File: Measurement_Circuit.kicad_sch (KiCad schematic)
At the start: 45 parts, among them IC1 ISO6721RBDR, J4 Screw_Terminal_01x03, J5 Screw_Terminal_01x03, J6 Screw_Terminal_01x02, U3 ADE7953xCP, U8 ISO1541, Y1 3.58 MHz

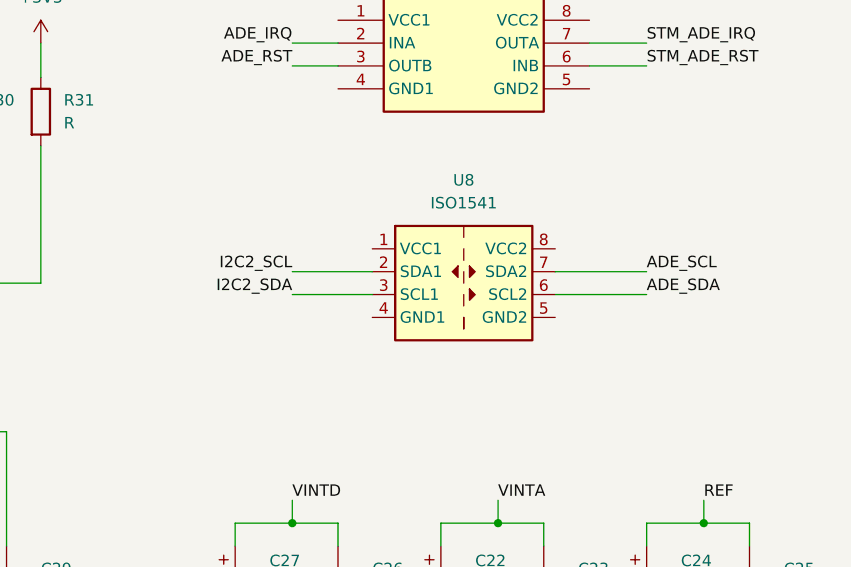
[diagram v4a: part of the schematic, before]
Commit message: I2C pullups
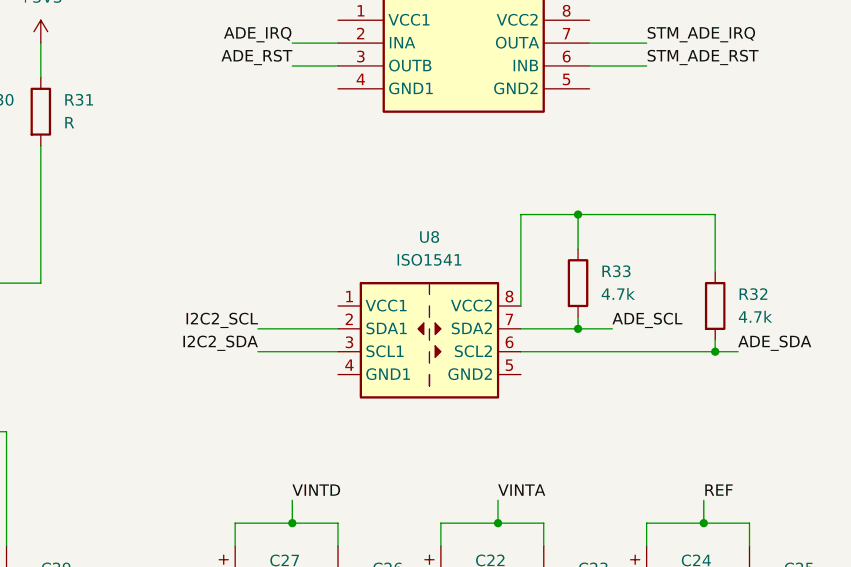
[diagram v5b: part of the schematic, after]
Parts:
- added R32, R33: 4.7k, symbol Device:R
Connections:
- net ADE_SCL: now also R33.2
- net ADE_SDA: now also R32.2
- net at U8.8 (VCC2): now also R32.1, R33.1
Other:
- moved on the sheet: U8
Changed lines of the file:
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@@
 (kicad_sch (version 20230121) (generator eeschema)
   (paper "A4")
+  (junction (at 236.22 64.77) (diameter 0) (color 0 0 0 0)
+  )
   (junction (at 158.75 99.06) (diameter 0) (color 0 0 0 0)
   )
@@
   (junction (at 63.5 55.88) (diameter 0) (color 0 0 0 0)
   )
+  (junction (at 251.46 80.01) (diameter 0) (color 0 0 0 0)
+  )
   (junction (at 78.74 44.45) (diameter 0) (color 0 0 0 0)
   )
@@
   )
   (junction (at 63.5 44.45) (diameter 0) (color 0 0 0 0)
+  )
+  (junction (at 236.22 77.47) (diameter 0) (color 0 0 0 0)
   )
   (junction (at 158.75 88.9) (diameter 0) (color 0 0 0 0)
@@
     (stroke (width 0) (type default))
   )
-  (wire (pts (xy 233.68 71.12) (xy 243.84 71.12))
+  (wire (pts (xy 229.87 77.47) (xy 236.22 77.47))
     (stroke (width 0) (type default))
   )
@@
     (stroke (width 0) (type default))
   )
+  (wire (pts (xy 251.46 80.01) (xy 254 80.01))
+    (stroke (width 0) (type default))
+  )
+  (wire (pts (xy 236.22 77.47) (xy 240.03 77.47))
+    (stroke (width 0) (type default))
+  )
   (wire (pts (xy 63.5 67.31) (xy 66.04 67.31))
     (stroke (width 0) (type default))
@@
     (stroke (width 0) (type default))
   )
+  (wire (pts (xy 251.46 64.77) (xy 251.46 71.12))
+    (stroke (width 0) (type default))
+  )
   (wire (pts (xy 255.27 101.6) (xy 255.27 99.06))
     (stroke (width 0) (type default))
@@
     (stroke (width 0) (type default))
   )
+  (wire (pts (xy 236.22 76.2) (xy 236.22 77.47))
+    (stroke (width 0) (type default))
+  )
   (wire (pts (xy 49.53 44.45) (xy 52.07 44.45))
     (stroke (width 0) (type default))
@@
     (stroke (width 0) (type default))
   )
-  (wire (pts (xy 233.68 73.66) (xy 243.84 73.66))
+  (wire (pts (xy 229.87 80.01) (xy 251.46 80.01))
     (stroke (width 0) (type default))
   )
@@
     (stroke (width 0) (type default))
   )
-  (wire (pts (xy 204.47 73.66) (xy 213.36 73.66))
-    (stroke (width 0) (type default))
-  )
-  (wire (pts (xy 204.47 71.12) (xy 213.36 71.12))
+  (wire (pts (xy 200.66 80.01) (xy 209.55 80.01))
+    (stroke (width 0) (type default))
+  )
+  (wire (pts (xy 200.66 77.47) (xy 209.55 77.47))
     (stroke (width 0) (type default))
   )
@@
     (stroke (width 0) (type default))
   )
+  (wire (pts (xy 251.46 78.74) (xy 251.46 80.01))
+    (stroke (width 0) (type default))
+  )
   (wire (pts (xy 63.5 54.61) (xy 63.5 55.88))
     (stroke (width 0) (type default))
@@
     (stroke (width 0) (type default))
   )
+  (wire (pts (xy 229.87 74.93) (xy 229.87 64.77))
+    (stroke (width 0) (type default))
+  )
   (wire (pts (xy 243.84 99.06) (xy 243.84 101.6))
     (stroke (width 0) (type default))
@@
     (stroke (width 0) (type default))
   )
+  (wire (pts (xy 236.22 64.77) (xy 251.46 64.77))
+    (stroke (width 0) (type default))
+  )
   (wire (pts (xy 63.5 101.6) (xy 66.04 101.6))
     (stroke (width 0) (type default))
@@
     (stroke (width 0) (type default))
   )
+  (wire (pts (xy 229.87 64.77) (xy 236.22 64.77))
+    (stroke (width 0) (type default))
+  )
   (wire (pts (xy 255.27 109.22) (xy 255.27 110.49))
     (stroke (width 0) (type default))
   )
   (wire (pts (xy 116.84 62.23) (xy 123.19 62.23))
+    (stroke (width 0) (type default))
+  )
+  (wire (pts (xy 236.22 64.77) (xy 236.22 68.58))
     (stroke (width 0) (type default))
   )
@@
     (effects (font (size 1.27 1.27)) (justify right bottom))
   )
-  (label "ADE_SDA" (at 243.84 73.66 0) (fields_autoplaced)
+  (label "ADE_SDA" (at 254 80.01 0) (fields_autoplaced)
     (effects (font (size 1.27 1.27)) (justify left bottom))
   )
@@
     (effects (font (size 1.27 1.27)) (justify left bottom))
   )
-  (label "I2C2_SDA" (at 204.47 73.66 180) (fields_autoplaced)
+  (label "I2C2_SDA" (at 200.66 80.01 180) (fields_autoplaced)
     (effects (font (size 1.27 1.27)) (justify right bottom))
   )
@@
     (effects (font (size 1.27 1.27)) (justify left bottom))
   )
-  (label "ADE_SCL" (at 243.84 71.12 0) (fields_autoplaced)
+  (label "ADE_SCL" (at 240.03 77.47 0) (fields_autoplaced)
     (effects (font (size 1.27 1.27)) (justify left bottom))
   )
@@
     (effects (font (size 1.27 1.27)) (justify left bottom))
   )
-  (label "I2C2_SCL" (at 204.47 71.12 180) (fields_autoplaced)
+  (label "I2C2_SCL" (at 200.66 77.47 180) (fields_autoplaced)
     (effects (font (size 1.27 1.27)) (justify right bottom))
   )
@@
     )
   )
-  (symbol (lib_id "Isolator:ISO1541") (at 223.52 71.12 0) (unit 1)
-    (in_bom yes) (on_board yes) (dnp no) (fields_autoplaced)
-    (property "Reference" "U8" (at 223.52 60.96 0)
-      (effects (font (size 1.27 1.27)))
-    )
-    (property "Value" "ISO1541" (at 223.52 63.5 0)
-      (effects (font (size 1.27 1.27)))
-    )
-    (property "Footprint" "Package_SO:SOIC-8_3.9x4.9mm_P1.27mm" (at 223.52 80.01 0)
-      (effects (font (size 1.27 1.27)) hide)
-    )
-    (property "Datasheet" "http://www.ti.com/lit/ds/symlink/iso1541.pdf" (at 223.52 69.85 0)
+  (symbol (lib_id "Isolator:ISO1541") (at 219.71 77.47 0) (unit 1)
+    (in_bom yes) (on_board yes) (dnp no) (fields_autoplaced)
+    (property "Reference" "U8" (at 219.71 67.31 0)
+      (effects (font (size 1.27 1.27)))
+    )
+    (property "Value" "ISO1541" (at 219.71 69.85 0)
+      (effects (font (size 1.27 1.27)))
+    )
+    (property "Footprint" "Package_SO:SOIC-8_3.9x4.9mm_P1.27mm" (at 219.71 86.36 0)
+      (effects (font (size 1.27 1.27)) hide)
+    )
+    (property "Datasheet" "http://www.ti.com/lit/ds/symlink/iso1541.pdf" (at 219.71 76.2 0)
       (effects (font (size 1.27 1.27)) hide)
     )
@@
     )
   )
+  (symbol (lib_id "Device:R") (at 236.22 72.39 0) (unit 1)
+    (in_bom yes) (on_board yes) (dnp no) (fields_autoplaced)
+    (property "Reference" "R33" (at 238.76 71.12 0)
+      (effects (font (size 1.27 1.27)) (justify left))
+    )
+    (property "Value" "4.7k" (at 238.76 73.66 0)
+      (effects (font (size 1.27 1.27)) (justify left))
+    )
+    (property "Footprint" "" (at 234.442 72.39 90)
+      (effects (font (size 1.27 1.27)) hide)
+    )
+    (property "Datasheet" "~" (at 236.22 72.39 0)
+      (effects (font (size 1.27 1.27)) hide)
+    )
+    (pin "1")
+    (pin "2")
+    (instances
+      (project "Eng_Thesis"
+        (path "/97bd1b5a-123d-47f8-a974-72569e0e2197"
+          (reference "R33") (unit 1)
+        )
+        (path "/97bd1b5a-123d-47f8-a974-72569e0e2197/169631cb-4600-41da-8cbe-8c1369144896"
+          (reference "R34") (unit 1)
+        )
+      )
+    )
+  )
   (symbol (lib_id "Device:R") (at 167.64 53.34 0) (unit 1)
     (in_bom yes) (on_board yes) (dnp no) (fields_autoplaced)
@@
         )
       )
+    )
+  )
+  (symbol (lib_id "Device:R") (at 251.46 74.93 0) (unit 1)
+    (in_bom yes) (on_board yes) (dnp no) (fields_autoplaced)
+    (property "Reference" "R32" (at 254 73.66 0)
+      (effects (font (size 1.27 1.27)) (justify left))
+    )
+    (property "Value" "4.7k" (at 254 76.2 0)
+      (effects (font (size 1.27 1.27)) (justify left))
+    )
+    (property "Footprint" "" (at 249.682 74.93 90)
+      (effects (font (size 1.27 1.27)) hide)
+    )
+    (property "Datasheet" "~" (at 251.46 74.93 0)
+      (effects (font (size 1.27 1.27)) hide)
+    )
+    (pin "1")
+    (pin "2")
+    (instances
+      (project "Eng_Thesis"
+        (path "/97bd1b5a-123d-47f8-a974-72569e0e2197"
+          (reference "R32") (unit 1)
+        )
+        (path "/97bd1b5a-123d-47f8-a974-72569e0e2197/169631cb-4600-41da-8cbe-8c1369144896"
+          (reference "R35") (unit 1)
+        )
+      )

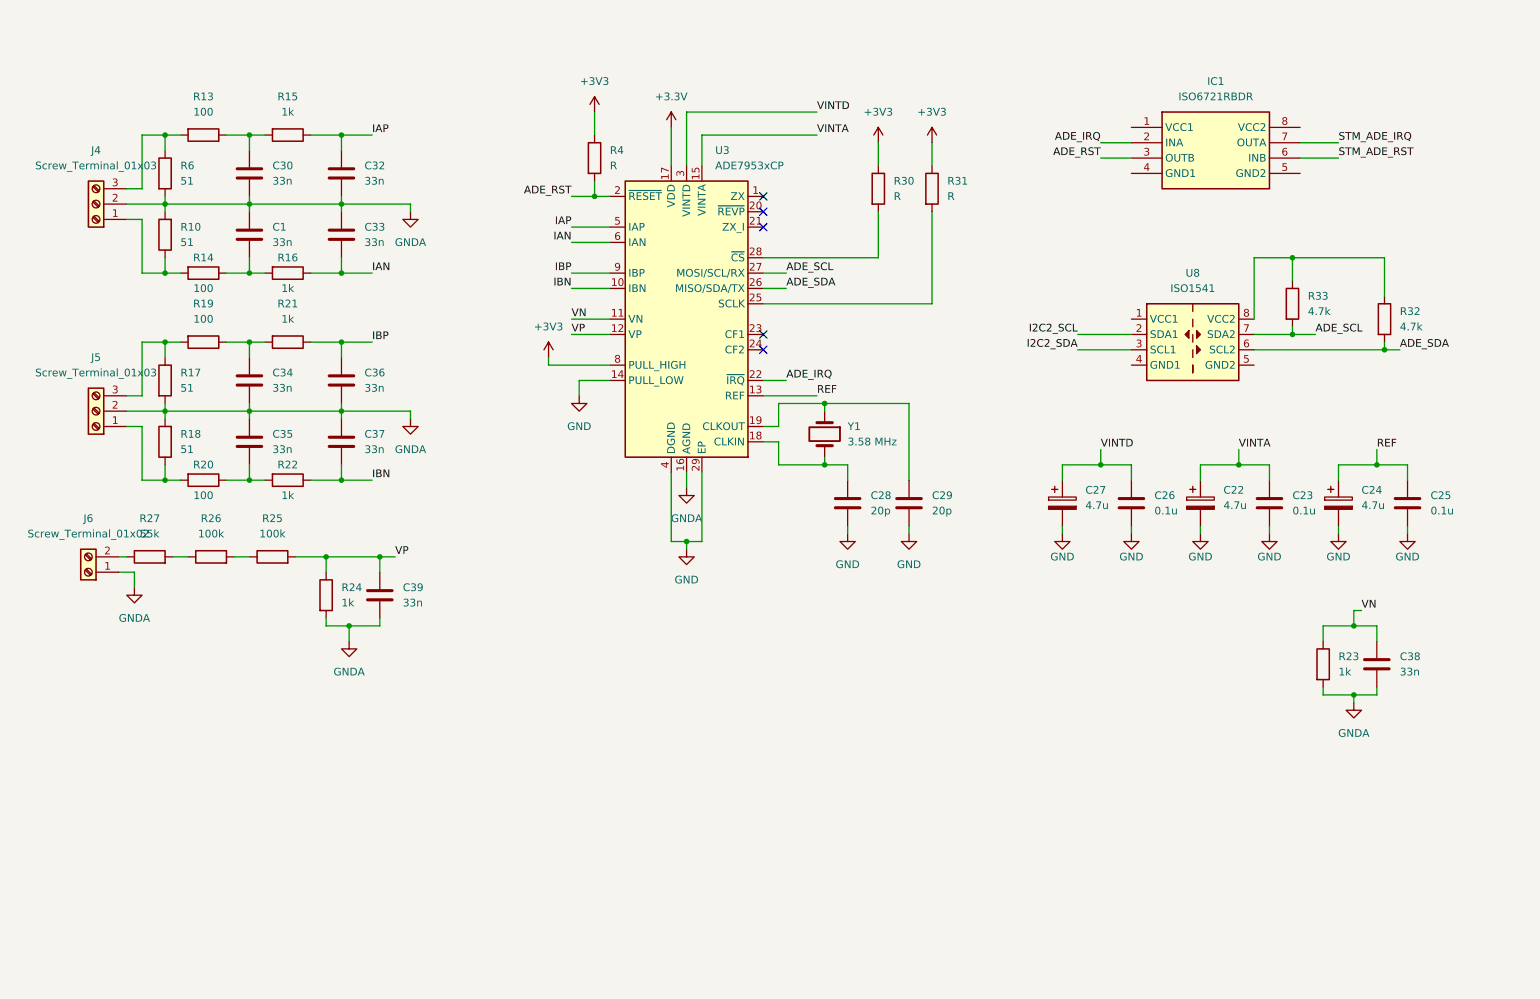
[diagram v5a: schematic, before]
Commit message: v0.1 of schematic + most of footprints/links
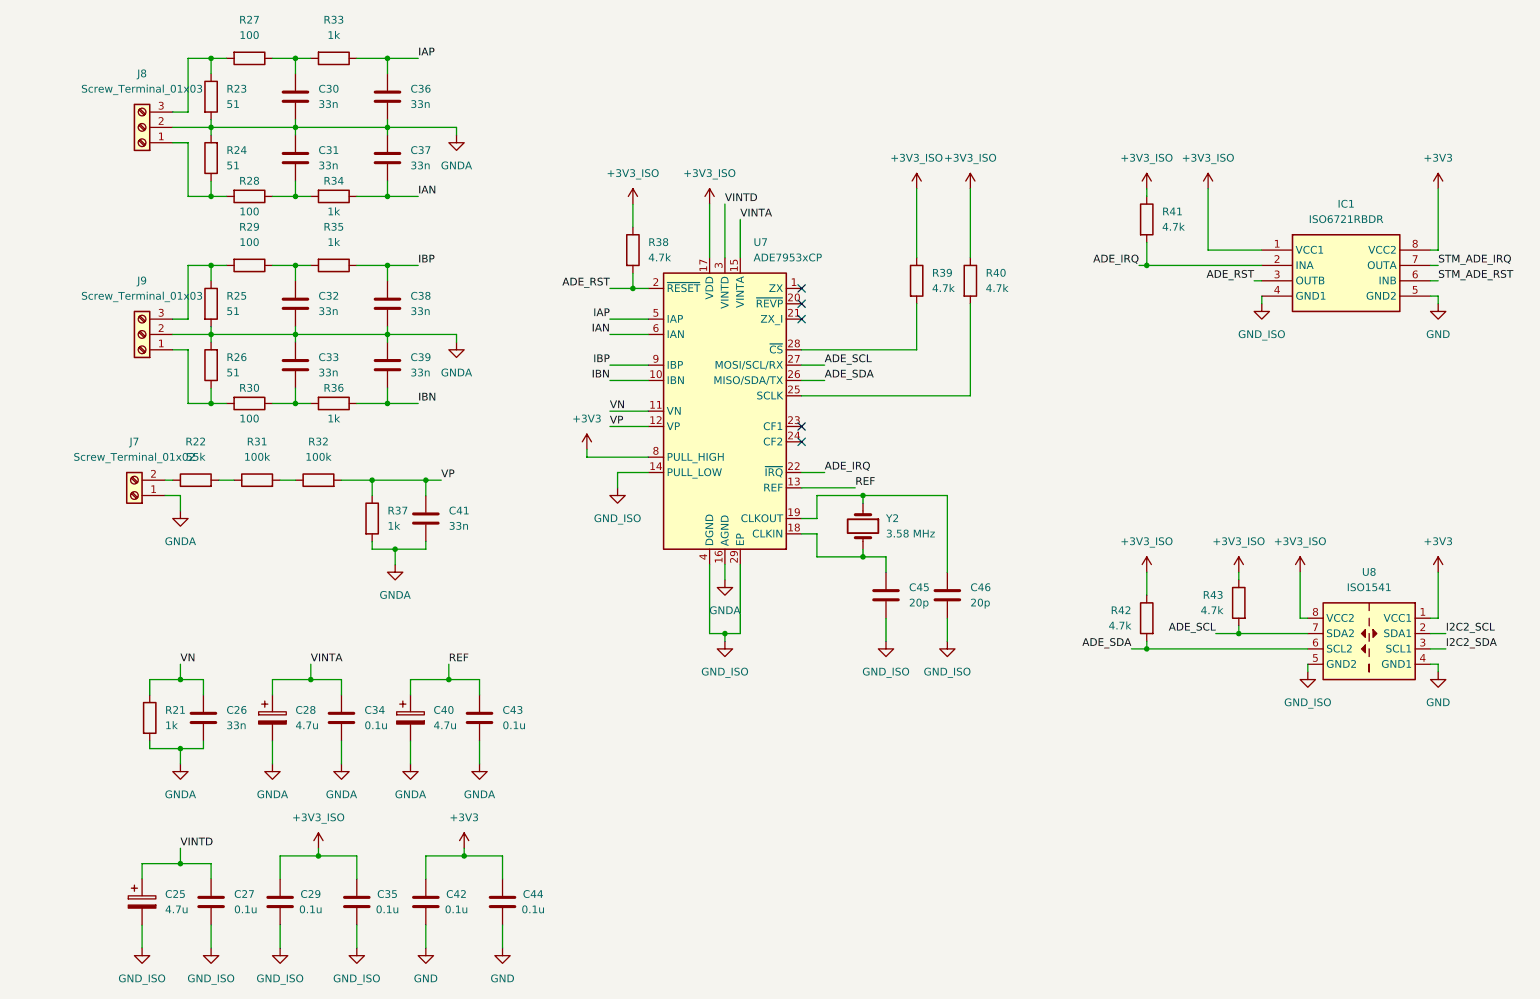
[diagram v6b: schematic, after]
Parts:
- removed C24, C27: 4.7u, symbol Device:C_Polarized
- added C25, C40: 4.7u, Capacitor_SMD:CP_Elec_4x5.4, symbol Device:C_Polarized
- added C35, C42, C44: 0.1u, Capacitor_SMD:C_0201_0603Metric_Pad0.64x0.40mm_HandSolder, symbol Device:C
- added C46: 20p, Capacitor_SMD:C_0603_1608Metric_Pad1.08x0.95mm_HandSolder, symbol Device:C
- added R41: 4.7k, symbol Device:R
- C26: renamed from C38; footprint (none) -> Capacitor_SMD:C_0603_1608Metric_Pad1.08x0.95mm_HandSolder
- C27: renamed from C26; footprint (none) -> Capacitor_SMD:C_0201_0603Metric_Pad0.64x0.40mm_HandSolder
- C28: renamed from C22; footprint (none) -> Capacitor_SMD:CP_Elec_4x5.4
- C29: value 20p -> 0.1u; footprint (none) -> Capacitor_SMD:C_0201_0603Metric_Pad0.64x0.40mm_HandSolder
- C30: footprint (none) -> Capacitor_SMD:C_0603_1608Metric_Pad1.08x0.95mm_HandSolder
- C31: renamed from C1; footprint (none) -> Capacitor_SMD:C_0603_1608Metric_Pad1.08x0.95mm_HandSolder
- C32: renamed from C34; footprint (none) -> Capacitor_SMD:C_0603_1608Metric_Pad1.08x0.95mm_HandSolder
- C33: renamed from C35; footprint (none) -> Capacitor_SMD:C_0603_1608Metric_Pad1.08x0.95mm_HandSolder
- C34: renamed from C23; footprint (none) -> Capacitor_SMD:C_0201_0603Metric_Pad0.64x0.40mm_HandSolder
- C36: renamed from C32; footprint (none) -> Capacitor_SMD:C_0603_1608Metric_Pad1.08x0.95mm_HandSolder
- C37: renamed from C33; footprint (none) -> Capacitor_SMD:C_0603_1608Metric_Pad1.08x0.95mm_HandSolder
- C38: renamed from C36; footprint (none) -> Capacitor_SMD:C_0603_1608Metric_Pad1.08x0.95mm_HandSolder
- C39: renamed from C37; footprint (none) -> Capacitor_SMD:C_0603_1608Metric_Pad1.08x0.95mm_HandSolder
- C41: renamed from C39; footprint (none) -> Capacitor_SMD:C_0603_1608Metric_Pad1.08x0.95mm_HandSolder
- C43: renamed from C25; footprint (none) -> Capacitor_SMD:C_0201_0603Metric_Pad0.64x0.40mm_HandSolder
- C45: renamed from C28; footprint (none) -> Capacitor_SMD:C_0603_1608Metric_Pad1.08x0.95mm_HandSolder
- IC1: footprint SOIC127P600X175-8N -> LibLoader:SOIC127P600X175-8N
- R38: renamed from R4; value R -> 4.7k
- R39: renamed from R30; value R -> 4.7k
- R40: renamed from R31; value R -> 4.7k
- renumbered J6 to J7, J4 to J8, J5 to J9, R23 to R21, R27 to R22, R6 to R23, R10 to R24, R17 to R25, R18 to R26, R13 to R27, R14 to R28, R19 to R29, R20 to R30, R26 to R31, R25 to R32, R15 to R33, R16 to R34, R21 to R35, R22 to R36, R24 to R37, R32 to R42, R33 to R43, U3 to U7, Y1 to Y2
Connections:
- net +3.3V is gone; now on net +3V3_ISO: U7.17 (VDD)
- net +3V3: now also IC1.8 (VCC2), U8.1 (VCC1), C42.2, C44.2; no longer R38.1, R39.1, R40.1
- net ADE_IRQ: now also R41.2
- net GND: now also IC1.5 (GND2), U8.4 (GND1), C42.1, C44.1; no longer C27.2, C28.2, C29.2, C34.2, C43.2, C45.2, U7.14 (PULL_LOW), U7.29 (EP), U7.4 (DGND)
- net GNDA: now also C28.2, C34.2, C43.2, C40.2
- net REF: now also C40.1
- net VINTD: now also C25.1
- net at U7.19 (CLKOUT), Y2.1: now also C46.1; no longer C29.1
- net GND_ISO: now reaches U8.5 (GND2)
- net GND_ISO: now also C27.2, C29.1, C45.2, IC1.4 (GND1), U7.14 (PULL_LOW), U7.29 (EP), U7.4 (DGND), C25.2, C35.1, C46.2
- net +3V3_ISO: now reaches R42.1, R43.1, U8.8 (VCC2)
- net +3V3_ISO: now also C29.2, IC1.1 (VCC1), R38.1, R39.1, R40.1, C35.2, R41.1
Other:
- moved on the sheet: C26, C27, C28, C30, C31, C32, C33, C34, C36, C37, C38, C39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
